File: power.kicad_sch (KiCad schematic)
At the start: 27 parts, among them J3 USB_C_Receptacle_USB2.0_16P, J5 +BATT, J6 -BATT, Q5 CJ3415, Q6 CJ2312, Q7 UMH3N, SW1 TSC02-TDW1FH3.5, U3 CP2104, U4 ADP2108AUJ-3.3, U5 TP4054

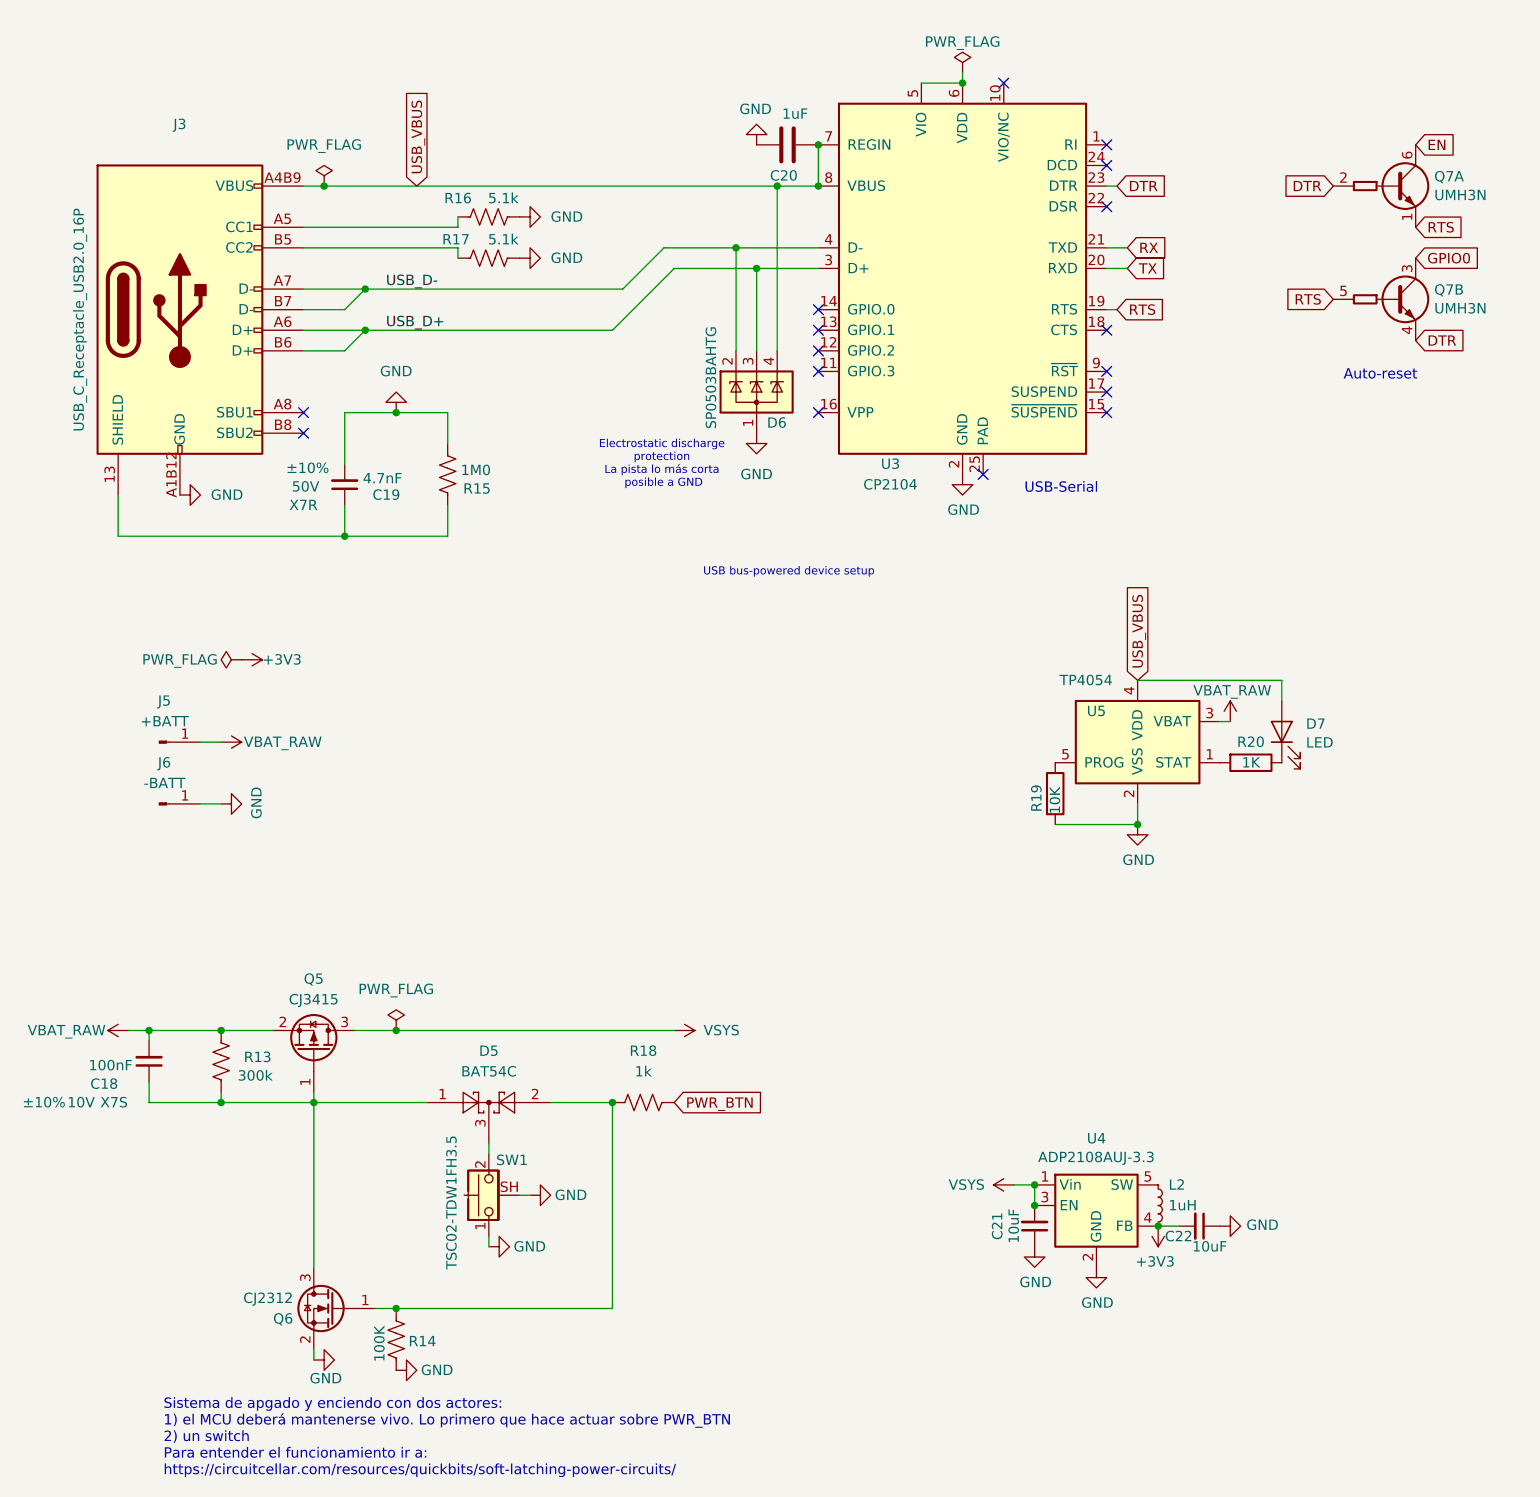
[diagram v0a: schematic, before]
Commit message: Consolida correcciones eléctricas y documentación
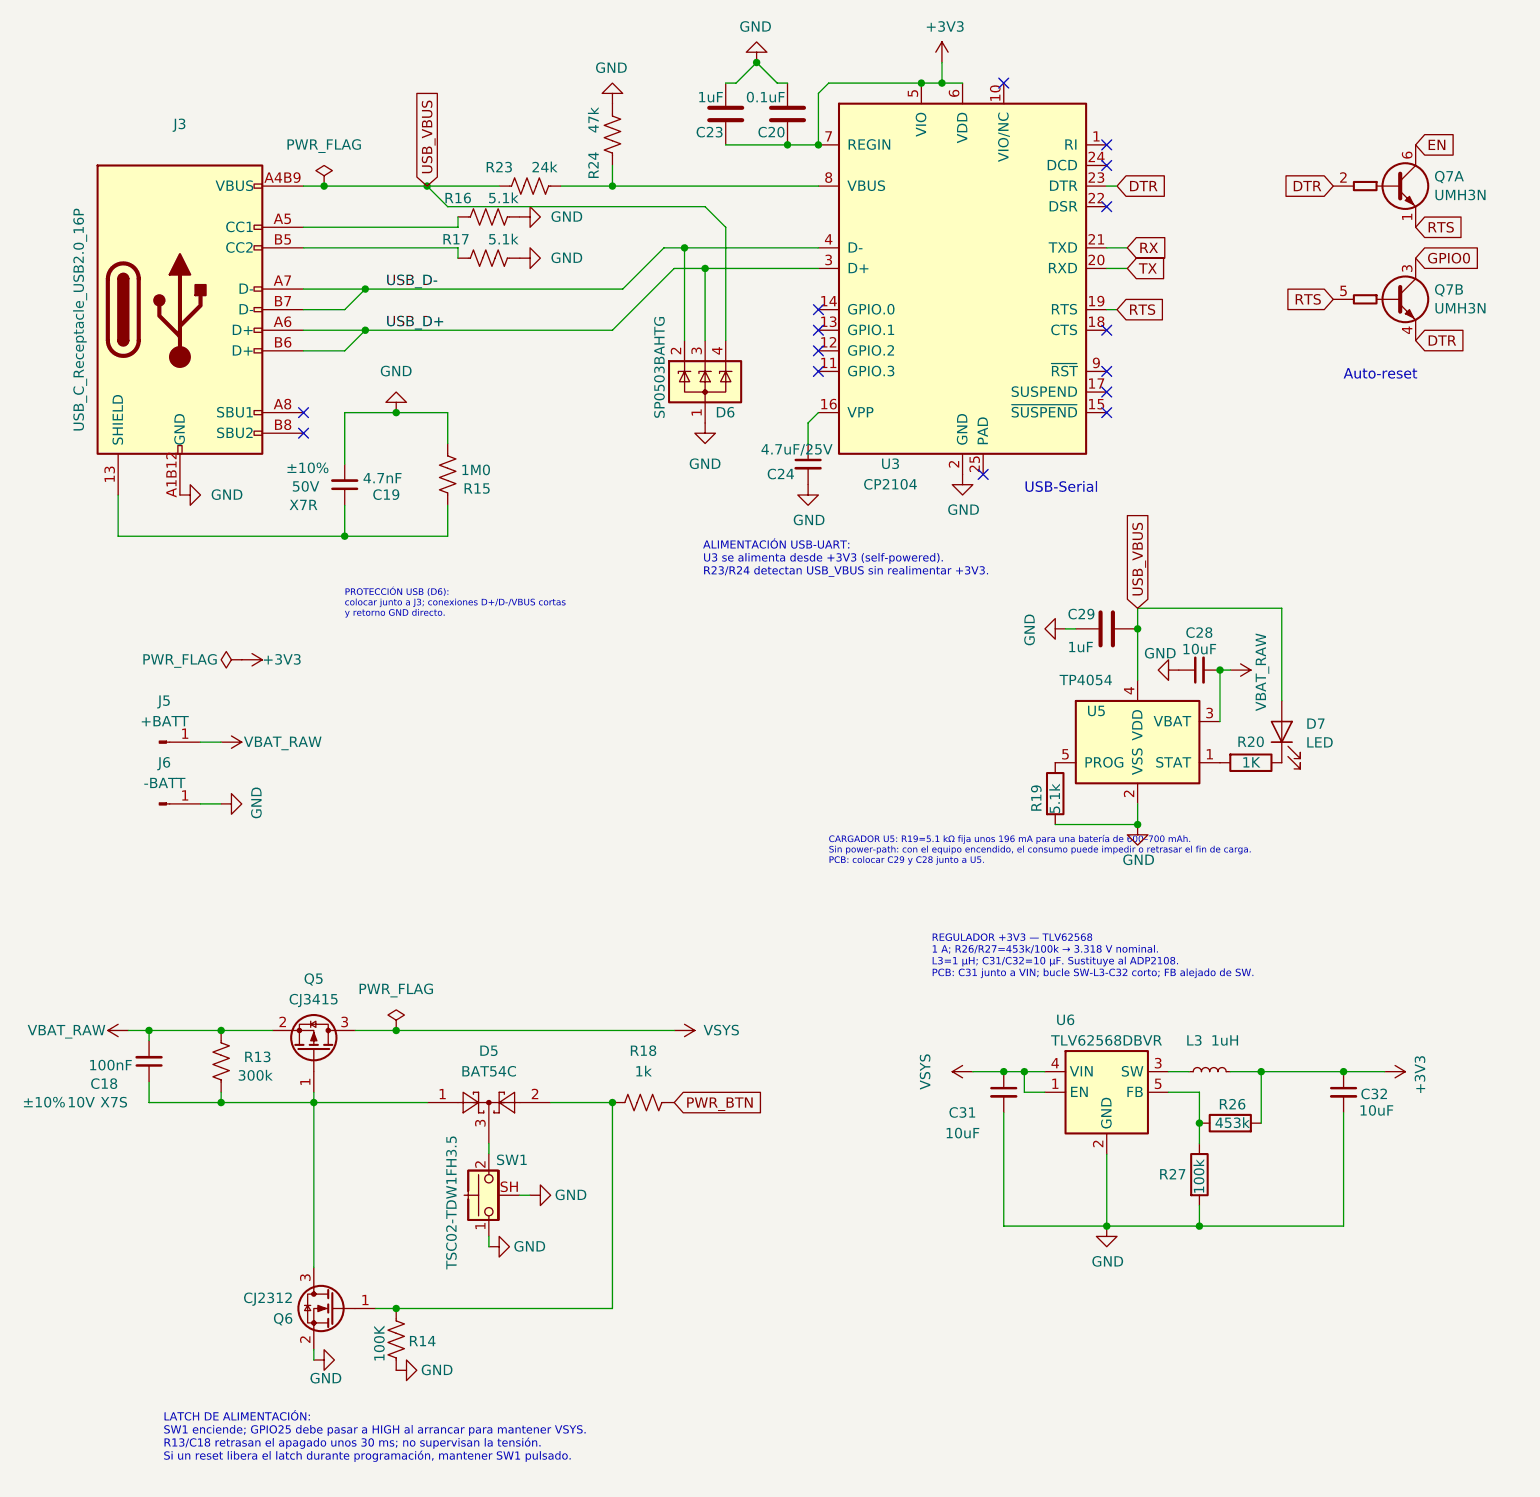
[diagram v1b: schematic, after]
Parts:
- removed C21, C22: 10uF, Capacitor_SMD:C_0603_1608Metric, symbol SmartFeedback-rescue:C_Small-Device
- removed L2: 1uH, Inductor_SMD:L_0805_2012Metric, symbol SmartFeedback-rescue:L_Small-Device
- removed U4: ADP2108AUJ-3.3, Package_TO_SOT_SMD:TSOT-23-5, symbol SmartFeedback-rescue:ADP2108AUJ-3.3-Regulator_Switching
- added C23, C29: 1uF, Capacitor_SMD:C_0603_1608Metric, symbol SmartFeedback-rescue:C-Device
- added C24: 4.7uF/25V, Capacitor_SMD:C_0603_1608Metric, symbol SmartFeedback-rescue:C_Small-Device
- added C28, C31, C32: 10uF, Capacitor_SMD:C_0603_1608Metric, symbol SmartFeedback-rescue:C_Small-Device
- added L3: 1uH, Inductor_SMD:L_Changjiang_FTC252012S, symbol SmartFeedback-rescue:L_Small-Device
- added R23: 24k, Resistor_SMD:R_0603_1608Metric, symbol Device:R_US
- added R24: 47k, Resistor_SMD:R_0603_1608Metric, symbol Device:R_US
- added R26: 453k, Resistor_SMD:R_0603_1608Metric, symbol SmartFeedback-rescue:R-Device
- added R27: 100k, Resistor_SMD:R_0603_1608Metric, symbol SmartFeedback-rescue:R-Device
- added U6: TLV62568DBVR, Package_TO_SOT_SMD:SOT-23-5, symbol Regulator_Switching:TLV62568DBV
- C18: LCSC Part # (none) -> C1525
- C19: LCSC Part # (none) -> C53987
- C20: value 1uF -> 0.1uF; LCSC Part # (none) -> C14663
- D5: LCSC Part C37704 -> (none); LCSC Part # (none) -> C22466350
- D6: LCSC Part # (none) -> C3040626
- D7: LCSC Part # (none) -> C84270
- J3: LCSC Part # (none) -> C2765186
- J5, J6: now left out of the parts list
- Q5: LCSC Part # (none) -> C2910186
- Q6: LCSC Part # (none) -> C23521
- Q7: LCSC Part # (none) -> C62892
- R13: LCSC Part # (none) -> C23024
- R14: LCSC Part # (none) -> C25803
- R15: LCSC Part # (none) -> C22935
- R16, R17: LCSC Part # (none) -> C23186
- R18, R20: LCSC Part # (none) -> C21190
- R19: value 10K -> 5.1k; LCSC Part # (none) -> C23186
- SW1: LCSC C22362983 -> (none); LCSC Part # (none) -> C22362983
- U3: LCSC Part # (none) -> C47742
- U5: LCSC Part # (none) -> C5381776
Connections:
- net +3V3: now also C20.1, U3.5 (VIO), U3.6 (VDD), U3.7 (REGIN), C23.1, C32.1, L3.2, R26.2
- net GND: now also C20.2, C23.2, C24.2, C28.1, C29.2, C31.2, C32.2, R24.2, R27.2, U6.2 (GND); no longer C20.1
- net USB_VBUS: now also C29.1, R23.1; no longer C20.2, U3.7 (REGIN), U3.8 (VBUS)
- net VBAT_RAW: now also C28.2
- net VSYS: now also C31.1, U6.1 (EN), U6.4 (VIN)
- net at U3.16 (VPP): now also C24.1
- new net: R26.1, R27.1, U6.5 (FB)
- new net: R23.2, R24.1, U3.8 (VBUS)
- new net: L3.1, U6.3 (SW)
- no-connect marks 16 -> 15
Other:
- note added: "ALIMENTACIÓN USB-UART: U3 se alimenta desde +3V3 (self-powered). R23/R24 detectan USB_VBUS sin realimentar +3V3."
- note added: "CARGADOR U5: R19=5.1 kΩ fija unos 196 mA para una batería de 600–700 mAh. Sin power-path: con el equipo encendido, el consumo puede impedir o retrasar el fin de carga. PCB: colocar C29 y C28 junto a U5."
- note added: "LATCH DE ALIMENTACIÓN: SW1 enciende; GPIO25 debe pasar a HIGH al arrancar para mantener VSYS. R13/C18 retrasan el apagado unos 30 ms; no supervisan la tensión. Si un reset libera el latch durante programación, mantener SW1 pulsado."
- note added: "PROTECCIÓN USB (D6): colocar junto a J3; conexiones D+/D-/VBUS cortas y retorno GND directo."
- note added: "REGULADOR +3V3 — TLV62568 1 A; R26/R27=453k/100k → 3.318 V nominal. L3=1 µH; C31/C32=10 µF. Sustituye al ADP2108. PCB: C31 junto a VIN; bucle SW-L3-C32 corto; FB alejado de SW."
- note removed: "Electrostatic discharge protection La pista lo más corta posible a GND"
- note removed: "Sistema de apgado y enciendo con dos actores: 1) el MCU deberá mantenerse vivo. Lo primero que hace actuar sobre PWR_BTN 2) un switch Para entender el funcionamiento ir a: https://circuitcellar.com/resources/quickbits/soft-latching-power-circuits/"
- note removed: "USB bus-powered device setup"
- moved on the sheet: C20, D6

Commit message: Aclara notas del esquema y valida salida de 3V3
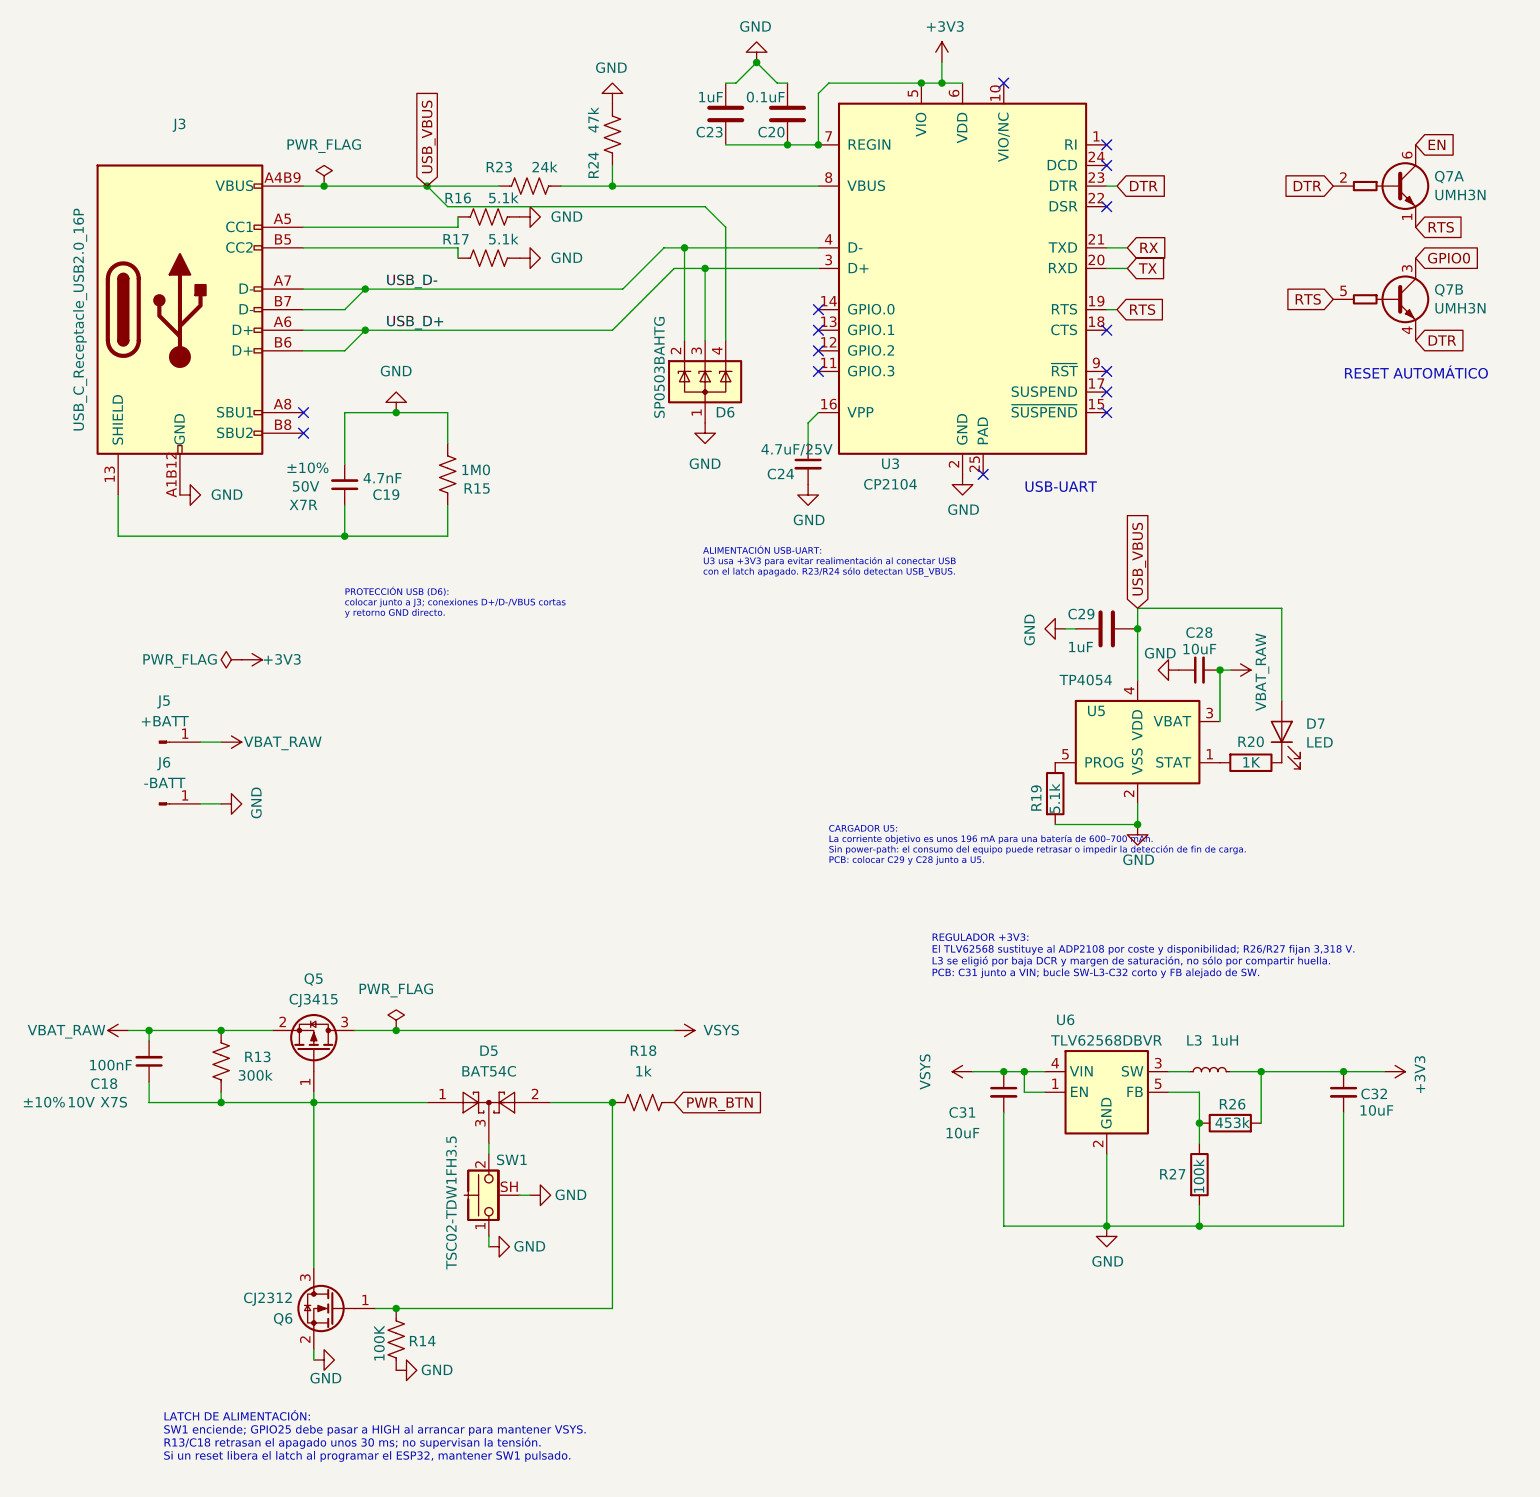
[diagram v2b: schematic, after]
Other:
- note added: "ALIMENTACIÓN USB-UART: U3 usa +3V3 para evitar realimentación al conectar USB con el latch apagado. R23/R24 sólo detectan USB_VBUS."
- note added: "CARGADOR U5: La corriente objetivo es unos 196 mA para una batería de 600–700 mAh. Sin power-path: el consumo del equipo puede retrasar o impedir la detección de fin de carga. PCB: colocar C29 y C28 junto a U5."
- note added: "LATCH DE ALIMENTACIÓN: SW1 enciende; GPIO25 debe pasar a HIGH al arrancar para mantener VSYS. R13/C18 retrasan el apagado unos 30 ms; no supervisan la tensión. Si un reset libera el latch al programar el ESP32, mantener SW1 pulsado."
- note added: "REGULADOR +3V3: El TLV62568 sustituye al ADP2108 por coste y disponibilidad; R26/R27 fijan 3,318 V. L3 se eligió por baja DCR y margen de saturación, no sólo por compartir huella. PCB: C31 junto a VIN; bucle SW-L3-C32 corto y FB alejado de SW."
- note added: "RESET AUTOMÁTICO"
- note added: "USB-UART"
- note removed: "ALIMENTACIÓN USB-UART: U3 se alimenta desde +3V3 (self-powered). R23/R24 detectan USB_VBUS sin realimentar +3V3."
- note removed: "Auto-reset"
- note removed: "CARGADOR U5: R19=5.1 kΩ fija unos 196 mA para una batería de 600–700 mAh. Sin power-path: con el equipo encendido, el consumo puede impedir o retrasar el fin de carga. PCB: colocar C29 y C28 junto a U5."
- note removed: "LATCH DE ALIMENTACIÓN: SW1 enciende; GPIO25 debe pasar a HIGH al arrancar para mantener VSYS. R13/C18 retrasan el apagado unos 30 ms; no supervisan la tensión. Si un reset libera el latch durante programación, mantener SW1 pulsado."
- note removed: "REGULADOR +3V3 — TLV62568 1 A; R26/R27=453k/100k → 3.318 V nominal. L3=1 µH; C31/C32=10 µF. Sustituye al ADP2108. PCB: C31 junto a VIN; bucle SW-L3-C32 corto; FB alejado de SW."
- note removed: "USB-Serial"
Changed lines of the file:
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@@
 		(company "MAmIoT")
 	)
-	(text "Auto-reset\n"
+	(text "RESET AUTOMÁTICO"
 		(exclude_from_sim no)
 		(at 179.07 57.15 0)
@@
 		)
 	)
-	(text "ALIMENTACIÓN USB-UART:\nU3 se alimenta desde +3V3 (self-powered).\nR23/R24 detectan USB_VBUS sin realimentar +3V3."
+	(text "ALIMENTACIÓN USB-UART:\nU3 usa +3V3 para evitar realimentación al conectar USB\ncon el latch apagado. R23/R24 sólo detectan USB_VBUS."
 		(exclude_from_sim no)
 		(at 100.076 81.28 0)
 		(effects
 			(font
-				(size 0.9906 0.9906)
+				(size 0.8 0.8)
 			)
 			(justify left bottom)
 		)
 	)
-	(text "\nUSB-Serial"
+	(text "USB-UART"
 		(exclude_from_sim no)
 		(at 139.7 71.12 0)
@@
 		)
 	)
-	(text "LATCH DE ALIMENTACIÓN:\nSW1 enciende; GPIO25 debe pasar a HIGH al arrancar para mantener VSYS.\nR13/C18 retrasan el apagado unos 30 ms; no supervisan la tensión.\nSi un reset libera el latch durante programación, mantener SW1 pulsado."
+	(text "LATCH DE ALIMENTACIÓN:\nSW1 enciende; GPIO25 debe pasar a HIGH al arrancar para mantener VSYS.\nR13/C18 retrasan el apagado unos 30 ms; no supervisan la tensión.\nSi un reset libera el latch al programar el ESP32, mantener SW1 pulsado."
 		(exclude_from_sim no)
 		(at 33.528 187.452 0)
@@
 		)
 	)
-	(text "REGULADOR +3V3 — TLV62568\n1 A; R26/R27=453k/100k → 3.318 V nominal.\nL3=1 µH; C31/C32=10 µF. Sustituye al ADP2108.\nPCB: C31 junto a VIN; bucle SW-L3-C32 corto; FB alejado de SW."
+	(text "REGULADOR +3V3:\nEl TLV62568 sustituye al ADP2108 por coste y disponibilidad; R26/R27 fijan 3,318 V.\nL3 se eligió por baja DCR y margen de saturación, no sólo por compartir huella.\nPCB: C31 junto a VIN; bucle SW-L3-C32 corto y FB alejado de SW."
 		(exclude_from_sim no)
 		(at 128.27 130.81 0)
@@
 		)
 	)
-	(text "CARGADOR U5: R19=5.1 kΩ fija unos 196 mA para una batería de 600–700 mAh.\nSin power-path: con el equipo encendido, el consumo puede impedir o retrasar el fin de carga.\nPCB: colocar C29 y C28 junto a U5."
+	(text "CARGADOR U5:\nLa corriente objetivo es unos 196 mA para una batería de 600–700 mAh.\nSin power-path: el consumo del equipo puede retrasar o impedir la detección de fin de carga.\nPCB: colocar C29 y C28 junto a U5."
 		(exclude_from_sim no)
 		(at 115.57 116.84 0)
